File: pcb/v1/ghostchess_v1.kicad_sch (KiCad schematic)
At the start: 16 parts, among them J1 CONN1, J2 CONN2, J3 CONN3, J4 CONN4, J9 POWER_IN, SW1 SS11-BBIWJ-R30-R, U66 AMS1117-3.3

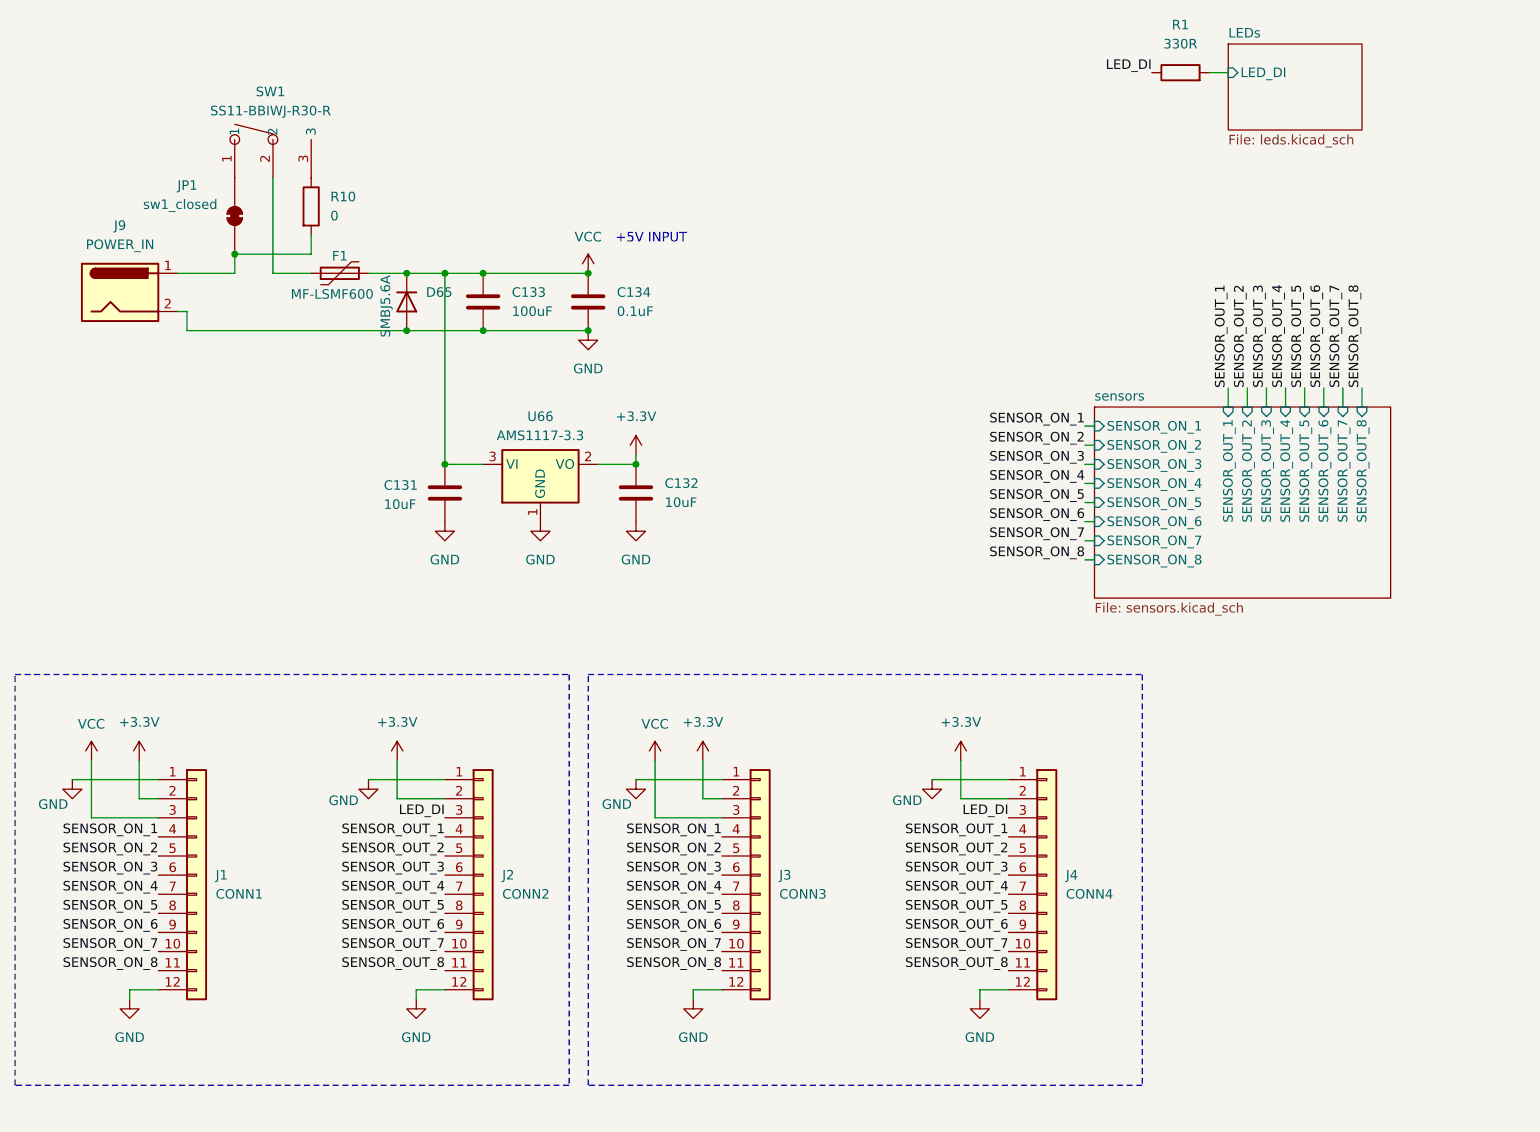
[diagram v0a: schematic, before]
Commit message: Add daughter board symbol
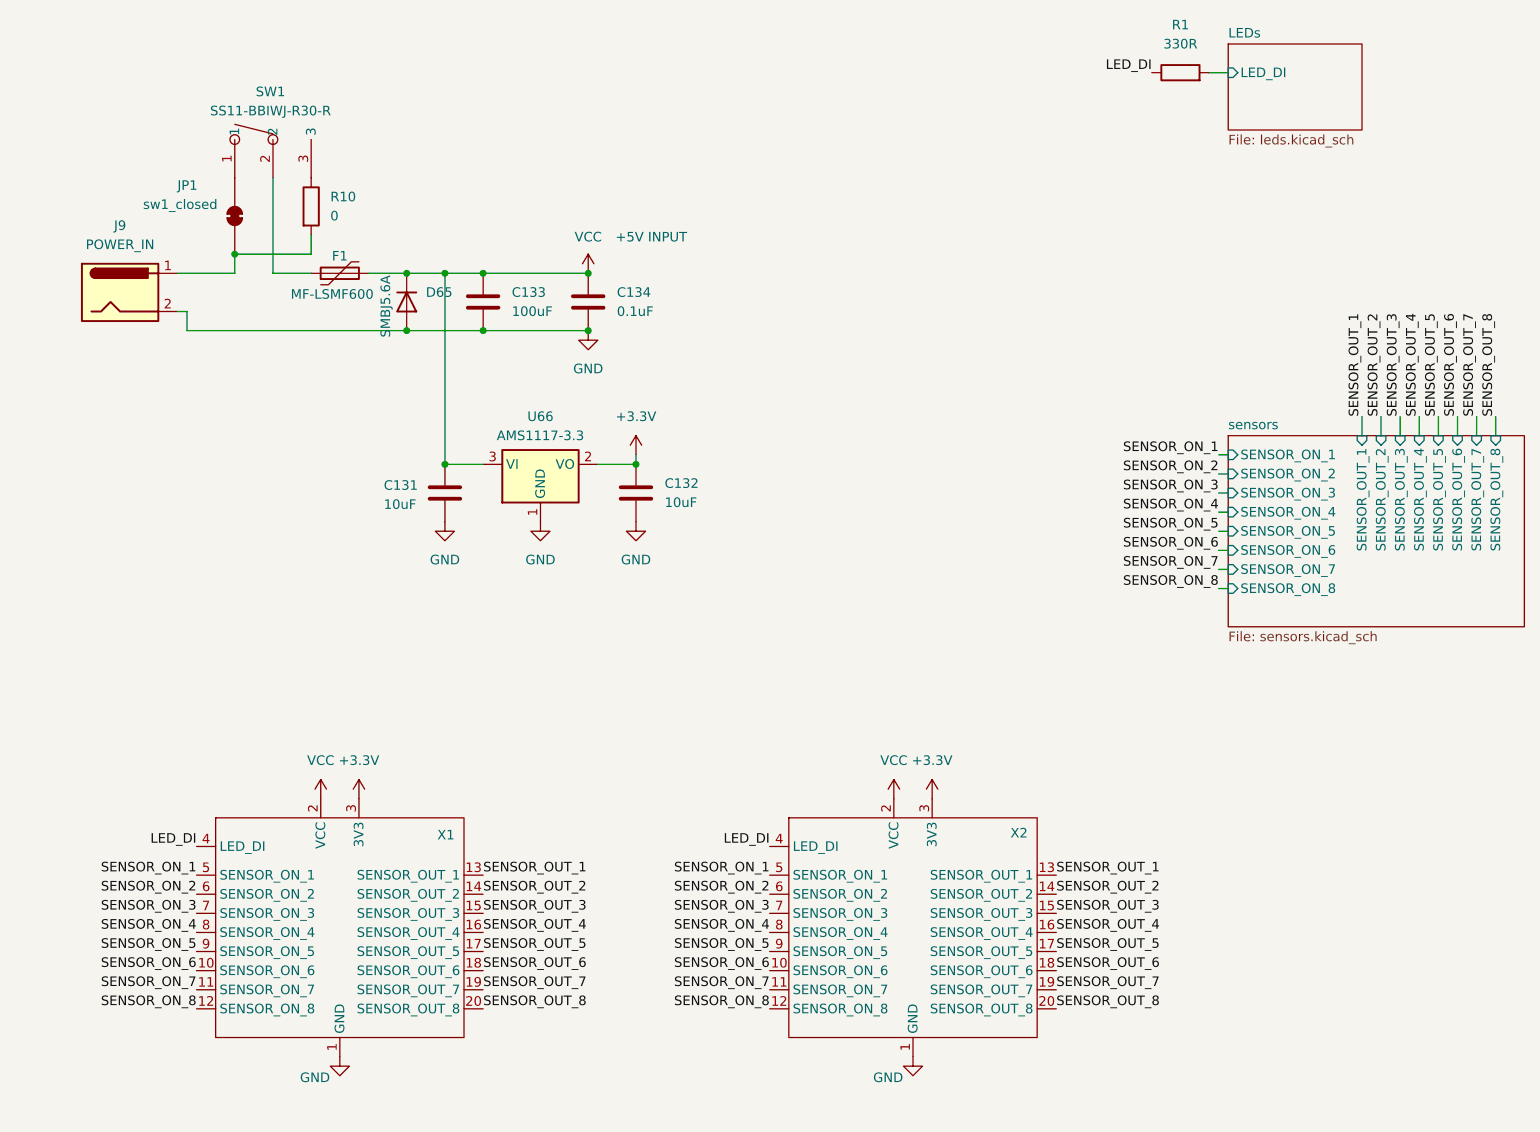
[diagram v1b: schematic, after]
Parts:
- removed J1: CONN1, Connector_PinHeader_2.54mm:PinHeader_1x12_P2.54mm_Vertical, symbol Connector_Generic:Conn_01x12
- removed J2: CONN2, Connector_PinHeader_2.54mm:PinHeader_1x12_P2.54mm_Vertical, symbol Connector_Generic:Conn_01x12
- removed J3: CONN3, Connector_PinHeader_2.54mm:PinHeader_1x12_P2.54mm_Vertical, symbol Connector_Generic:Conn_01x12
- removed J4: CONN4, Connector_PinHeader_2.54mm:PinHeader_1x12_P2.54mm_Vertical, symbol Connector_Generic:Conn_01x12
- added X1, X2: (no value), symbol ghostchess:ghostchess_daughter_board
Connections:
- net +3.3V: now also X1.3 (3V3), X2.3 (3V3)
- net GND: now also X1.1 (GND), X2.1 (GND)
- net LED_DI: now also X1.4 (LED_DI), X2.4 (LED_DI)
- net SENSOR_ON_1: now also X1.5 (SENSOR_ON_1), X2.5 (SENSOR_ON_1)
- net SENSOR_ON_2: now also X1.6 (SENSOR_ON_2), X2.6 (SENSOR_ON_2)
- net SENSOR_ON_3: now also X1.7 (SENSOR_ON_3), X2.7 (SENSOR_ON_3)
- net SENSOR_ON_4: now also X1.8 (SENSOR_ON_4), X2.8 (SENSOR_ON_4)
- net SENSOR_ON_5: now also X1.9 (SENSOR_ON_5), X2.9 (SENSOR_ON_5)
- net SENSOR_ON_6: now also X1.10 (SENSOR_ON_6), X2.10 (SENSOR_ON_6)
- net SENSOR_ON_7: now also X1.11 (SENSOR_ON_7), X2.11 (SENSOR_ON_7)
- net SENSOR_ON_8: now also X1.12 (SENSOR_ON_8), X2.12 (SENSOR_ON_8)
- net SENSOR_OUT_1: now also X1.13 (SENSOR_OUT_1), X2.13 (SENSOR_OUT_1)
- net SENSOR_OUT_2: now also X1.14 (SENSOR_OUT_2), X2.14 (SENSOR_OUT_2)
- net SENSOR_OUT_3: now also X1.15 (SENSOR_OUT_3), X2.15 (SENSOR_OUT_3)
- net SENSOR_OUT_4: now also X1.16 (SENSOR_OUT_4), X2.16 (SENSOR_OUT_4)
- net SENSOR_OUT_5: now also X1.17 (SENSOR_OUT_5), X2.17 (SENSOR_OUT_5)
- net SENSOR_OUT_6: now also X1.18 (SENSOR_OUT_6), X2.18 (SENSOR_OUT_6)
- net SENSOR_OUT_7: now also X1.19 (SENSOR_OUT_7), X2.19 (SENSOR_OUT_7)
- net SENSOR_OUT_8: now also X1.20 (SENSOR_OUT_8), X2.20 (SENSOR_OUT_8)
- net VCC: now also X1.2 (VCC), X2.2 (VCC)

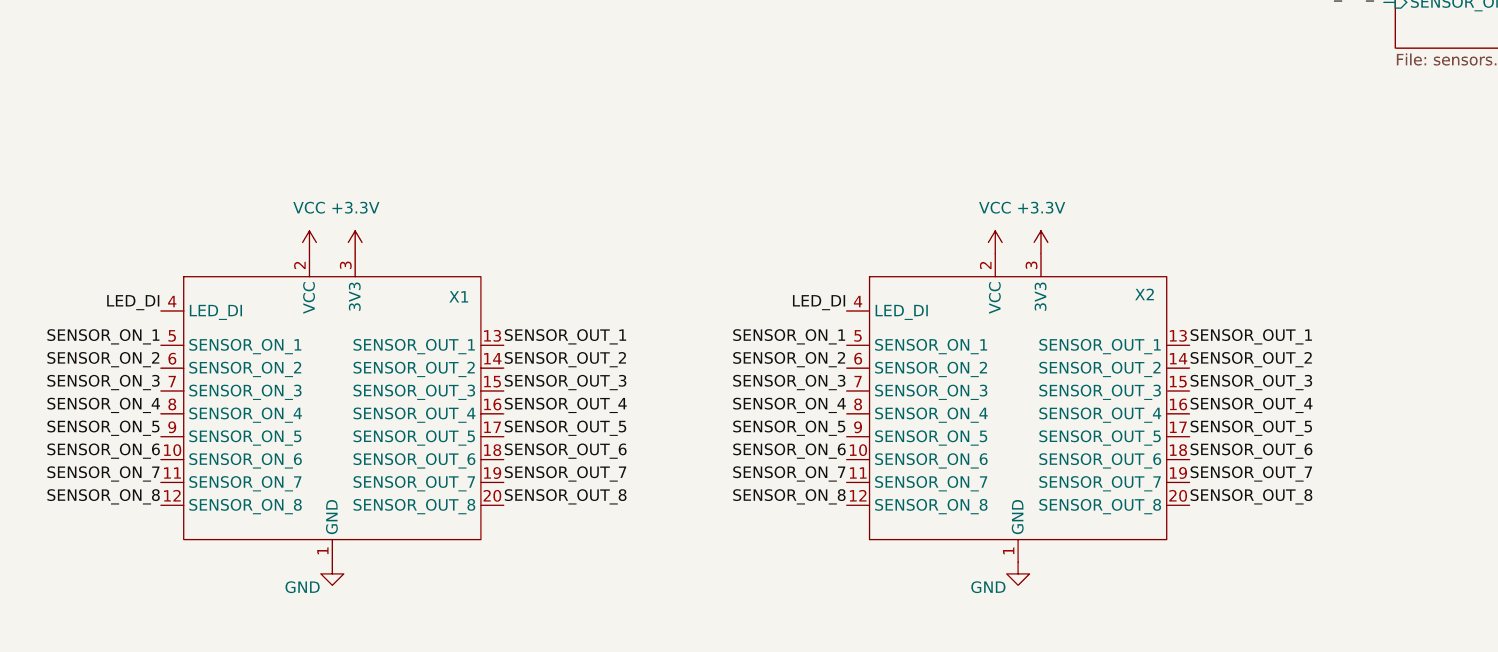
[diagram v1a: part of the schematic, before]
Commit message: Daughterboard footprints, more layout work
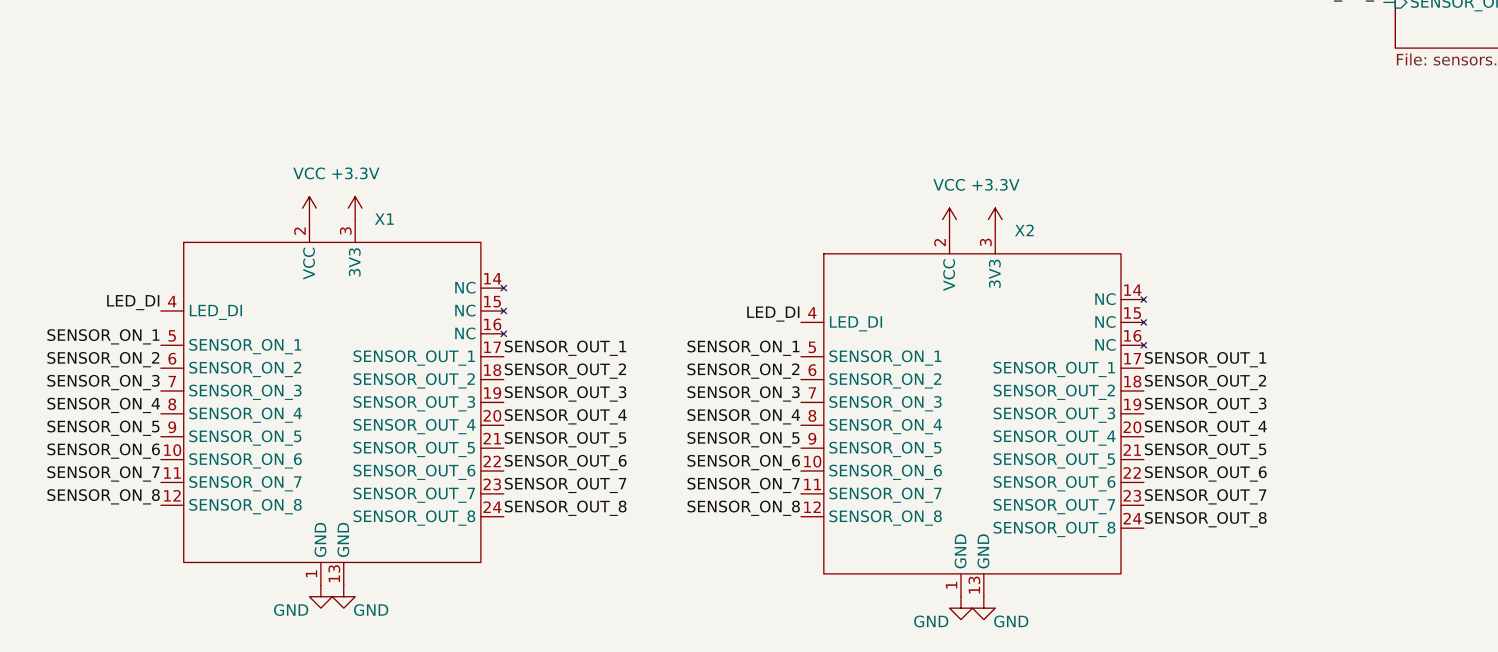
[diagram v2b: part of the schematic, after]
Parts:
- X1, X2: footprint (none) -> ghostchess:GhostChess_Daughter_Board
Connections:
- net GND: now also X1.13 (GND), X2.13 (GND)
- net SENSOR_OUT_1: now also X1.17 (SENSOR_OUT_1), X2.17 (SENSOR_OUT_1); no longer X1.13 (SENSOR_OUT_1), X2.13 (SENSOR_OUT_1)
- net SENSOR_OUT_2: now also X1.18 (SENSOR_OUT_2), X2.18 (SENSOR_OUT_2); no longer X1.14 (SENSOR_OUT_2), X2.14 (SENSOR_OUT_2)
- net SENSOR_OUT_3: now also X1.19 (SENSOR_OUT_3), X2.19 (SENSOR_OUT_3); no longer X1.15 (SENSOR_OUT_3), X2.15 (SENSOR_OUT_3)
- net SENSOR_OUT_4: now also X1.20 (SENSOR_OUT_4), X2.20 (SENSOR_OUT_4); no longer X1.16 (SENSOR_OUT_4), X2.16 (SENSOR_OUT_4)
- net SENSOR_OUT_5: now also X1.21 (SENSOR_OUT_5), X2.21 (SENSOR_OUT_5); no longer X1.17 (SENSOR_OUT_5), X2.17 (SENSOR_OUT_5)
- net SENSOR_OUT_6: now also X1.22 (SENSOR_OUT_6), X2.22 (SENSOR_OUT_6); no longer X1.18 (SENSOR_OUT_6), X2.18 (SENSOR_OUT_6)
- net SENSOR_OUT_7: now also X1.23 (SENSOR_OUT_7), X2.23 (SENSOR_OUT_7); no longer X1.19 (SENSOR_OUT_7), X2.19 (SENSOR_OUT_7)
- net SENSOR_OUT_8: now also X1.24 (SENSOR_OUT_8), X2.24 (SENSOR_OUT_8); no longer X1.20 (SENSOR_OUT_8), X2.20 (SENSOR_OUT_8)

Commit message: Continue PCB layout
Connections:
- net USER1: now reaches X1.14 (USER1)
- net USER1: now also X2.14 (USER1)
- net USER2: now reaches X1.15 (USER2)
- net USER2: now also X2.15 (USER2)
- net USER3: now reaches X1.16 (USER3)
- net USER3: now also X2.16 (USER3)
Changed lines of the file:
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@@
+		)
+	)
+	(label "USER3"
+		(at 85.09 135.89 0)
+		(effects
+			(font
+				(size 1.27 1.27)
+			)
+			(justify left bottom)
 		)
 	)
@@
 		)
 	)
+	(label "USER1"
+		(at 85.09 130.81 0)
+		(effects
+			(font
+				(size 1.27 1.27)
+			)
+			(justify left bottom)
+		)
+	)
 	(label "SENSOR_OUT_5"
 		(at 212.09 76.2 90)
@@
 		)
 	)
+	(label "USER1"
+		(at 156.21 132.08 0)
+		(effects
+			(font
+				(size 1.27 1.27)
+			)
+			(justify left bottom)
+		)
+	)
 	(label "SENSOR_ON_8"
 		(at 118.11 156.21 180)
@@
 		)
 	)
+	(label "USER3"
+		(at 156.21 137.16 0)
+		(effects
+			(font
+				(size 1.27 1.27)
+			)
+			(justify left bottom)
+		)
+	)
 	(label "SENSOR_ON_1"
 		(at 118.11 138.43 180)
@@
 		)
 	)
+	(label "USER2"
+		(at 156.21 134.62 0)
+		(effects
+			(font
+				(size 1.27 1.27)
+			)
+			(justify left bottom)
+		)
+	)
 	(label "SENSOR_OUT_2"
 		(at 156.21 142.24 0)
@@
 		)
 	)
+	(label "USER2"
+		(at 85.09 133.35 0)
+		(effects
+			(font
+				(size 1.27 1.27)
+			)
+			(justify left bottom)
+		)
+	)
